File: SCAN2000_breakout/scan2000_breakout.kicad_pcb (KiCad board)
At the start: 2 copper layers, 112 x 112 mm, 114 parts, among them J1 Banana socket, J10 Banana socket, J11 Banana socket, J12 Banana socket, J13 Banana socket, J14 Banana socket, J15 Banana socket, J16 Banana socket, J17 Banana socket, J18 Banana socket, J19 Banana socket, J2 Banana socket, J20 Banana socket, J21 IDC-Header_2x13, J22 Conn_02x10_Odd_Even, J23 Conn_01x02_Pin, J24 Conn_01x02_Pin, J3 Banana socket, J4 Banana socket, J5 Banana socket, J6 Banana socket, J7 Banana socket, J8 Banana socket, J9 Banana socket, U1 TLP3558A, U10 TLP3558A, U11 TLP3558A, U12 TLP3558A, U13 TLP3558A, U14 TLP3558A, U15 TLP3558A, U16 TLP3558A, U17 TLP3558A, U18 TLP3558A, U19 TLP3558A, U2 TLP3558A, U20 TLP3558A, U21 TLP3558A, U22 TLP3558A, U23 TLP3558A, U24 TLP3558A, U25 TLP3558A, U26 TLP3558A, U27 TLP3558A, U28 TLP3558A, U29 TLP3558A, U3 TLP3558A, U30 TLP3558A, U31 TLP3558A, U32 TLP3558A, U33 TLP3558A, U34 TLP3558A, U35 TLP3558A, U36 TLP3558A, U37 TLP3558A, U38 TLP3558A, U39 TLP3558A, U4 TLP3558A, U40 TLP3558A, U41 TLP3558A, U42 TLP3558A, U43 TLP3558A, U44 TLP3558A, U5 TLP3558A, U6 TLP3558A, U7 TLP3558A, U8 TLP3558A, U9 TLP3558A

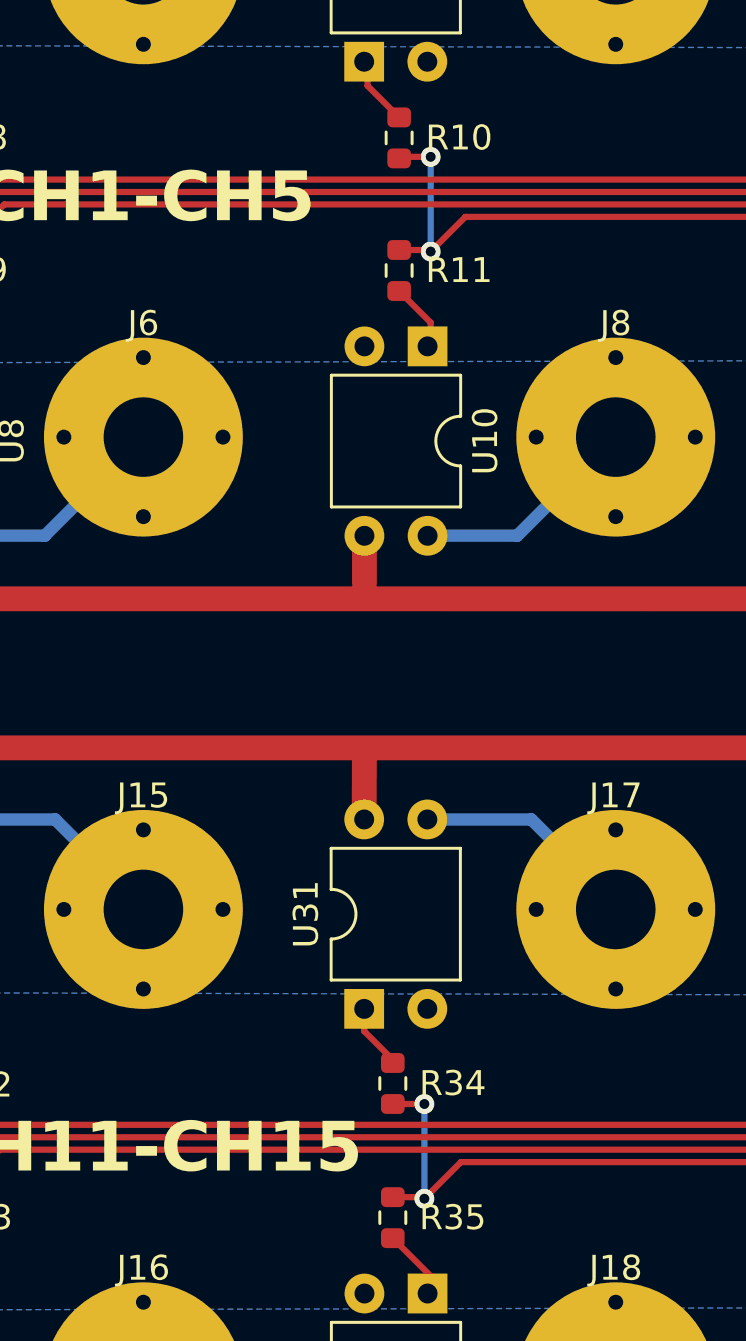
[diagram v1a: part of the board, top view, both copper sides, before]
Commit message: small silkscreen change
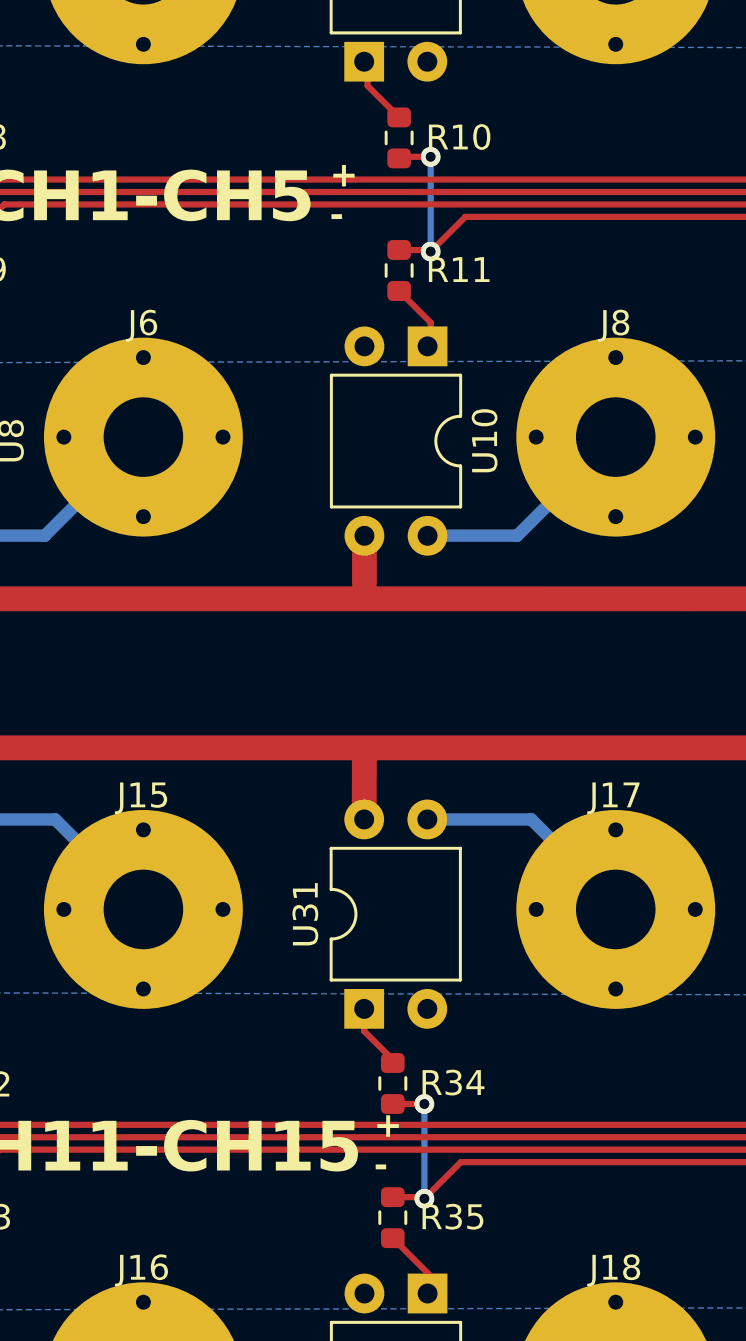
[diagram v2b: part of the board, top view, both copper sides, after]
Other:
- board text added: "+ -"
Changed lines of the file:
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@@
     (effects (font (size 2 2) (thickness 0.4) bold) (justify right))
+  )
+  (gr_text "+\n-" (at 104.27 86.874) (layer "F.SilkS")
+    (effects (font (size 1 1) (thickness 0.2) bold) (justify left bottom))
   )
   (gr_text "OUT -\nOUT +" (at 144.1025 128.77) (layer "F.SilkS")
@@
     (effects (font (size 2 2) (thickness 0.4) bold) (justify bottom))
   )
+  (gr_text "+\n-" (at 102.492 48.647) (layer "F.SilkS")
+    (effects (font (size 1 1) (thickness 0.2) bold) (justify left bottom))
+  )
   (segment (start 72.1992 34.28) (end 76.076 38.1568) (width 0.5) (layer "B.Cu") (net 3))

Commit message: Updates after fabrication
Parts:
- R1, R14: value 0.05 -> 0.1
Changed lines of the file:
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@@
     (tags "shunt resistor 4 contacts")
     (property "MFN" "Ohmite")
-    (property "PN" "LVK12R050DER")
+    (property "PN" "LVK12R100CER")
     (property "Sheetfile" "scan2000_breakout.kicad_sch")
     (property "Sheetname" "")
@@
         (effects (font (size 1 1) (thickness 0.15)))
     )
-    (fp_text value "0.05" (at 0 3.4) (layer "F.Fab")
+    (fp_text value "0.1" (at 0 3.4) (layer "F.Fab")
         (effects (font (size 1 1) (thickness 0.15)))
     )
@@
     (descr "Through hole IDC header, 2x13, 2.54mm pitch, DIN 41651 / IEC 60603-13, double rows latches, https://docs.google.com/spreadsheets/d/16SsEcesNF15N3Lb4niX7dcUr-NY5_MFPQhobNuNppn4/edit#gid=0")
     (tags "Through hole horizontal IDC header THT 2x13 2.54mm double row")
-    (property "MFN" "Würth")
-    (property "PN" "61202622121")
+    (property "MFN" "Amphenol")
+    (property "PN" "71922-126LF")
     (property "Sheetfile" "scan2000_breakout.kicad_sch")
     (property "Sheetname" "")
@@
       (rotate (xyz 0 0 0))
     )
-    (model "${KIPRJMOD}/project_specific_libs/61202622121.stp"
-      (offset (xyz 4.35 -15.2 3.5))
-      (scale (xyz 1 1 1))
-      (rotate (xyz 90 0 90))
+    (model "${KIPRJMOD}/project_specific_libs/71922_y26_asm.stp"
+      (offset (xyz -7.65 -84.56 7.1))
+      (scale (xyz 1 1 1))
+      (rotate (xyz -90 -90 0))
     )
   )
@@
     (tags "shunt resistor 4 contacts")
     (property "MFN" "Ohmite")
-    (property "PN" "LVK12R050DER")
+    (property "PN" "LVK12R100CER")
     (property "Sheetfile" "scan2000_breakout.kicad_sch")
     (property "Sheetname" "")
@@
         (effects (font (size 1 1) (thickness 0.15)))
     )
-    (fp_text value "0.05" (at 0 3.4) (layer "F.Fab")
-        (effects (font (size 1 1) (thickness 0.15)))
-    )
+    (fp_text value "0.1" (at 0 3.4) (layer "F.Fab")
+        (effects (font (size 1 1) (thickness 0.15)))
+    )
